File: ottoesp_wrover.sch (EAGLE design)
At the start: 45 parts, among them J1 DC-005, J2 2x3p-2.54, J3 4p-2.54, Q1 S8050, Q2 S8050, Q3 CJ2302, U2 CP2102, U3 CJA1117B-3.3-SOT89, U4 TPD4S012DRYR

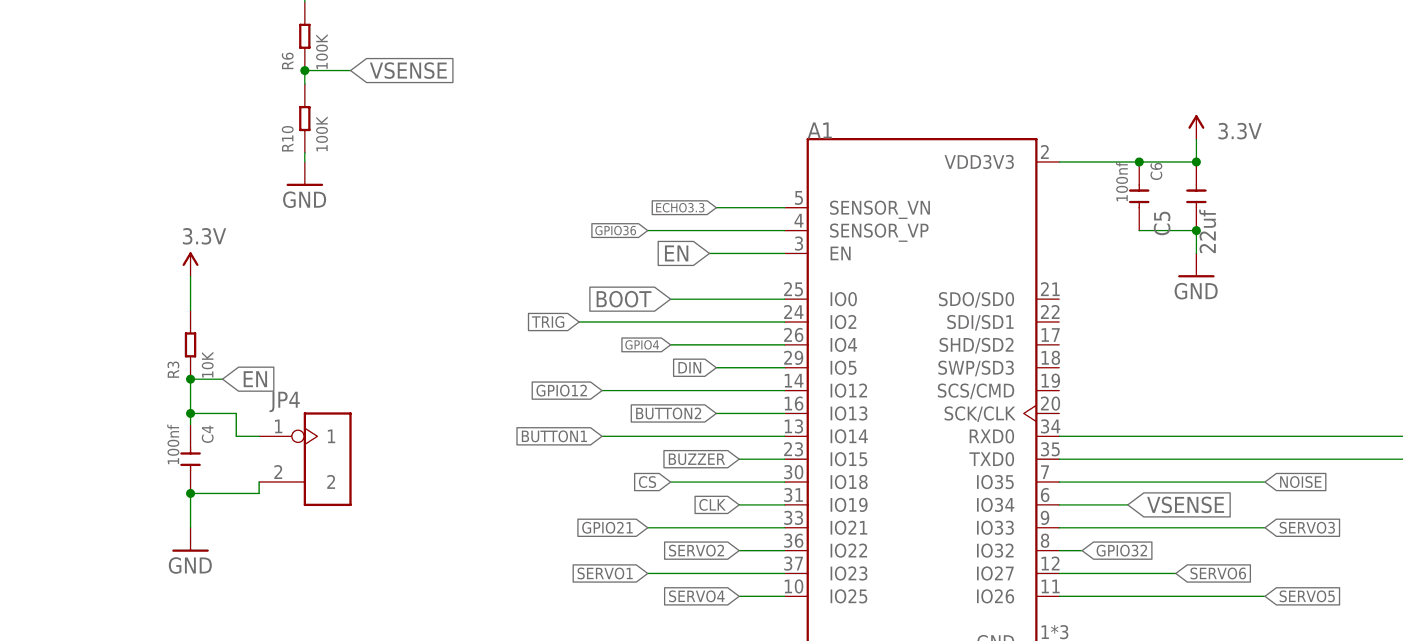
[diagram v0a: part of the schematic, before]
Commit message: Updated cap. These have been produced and seem to work. Still testing
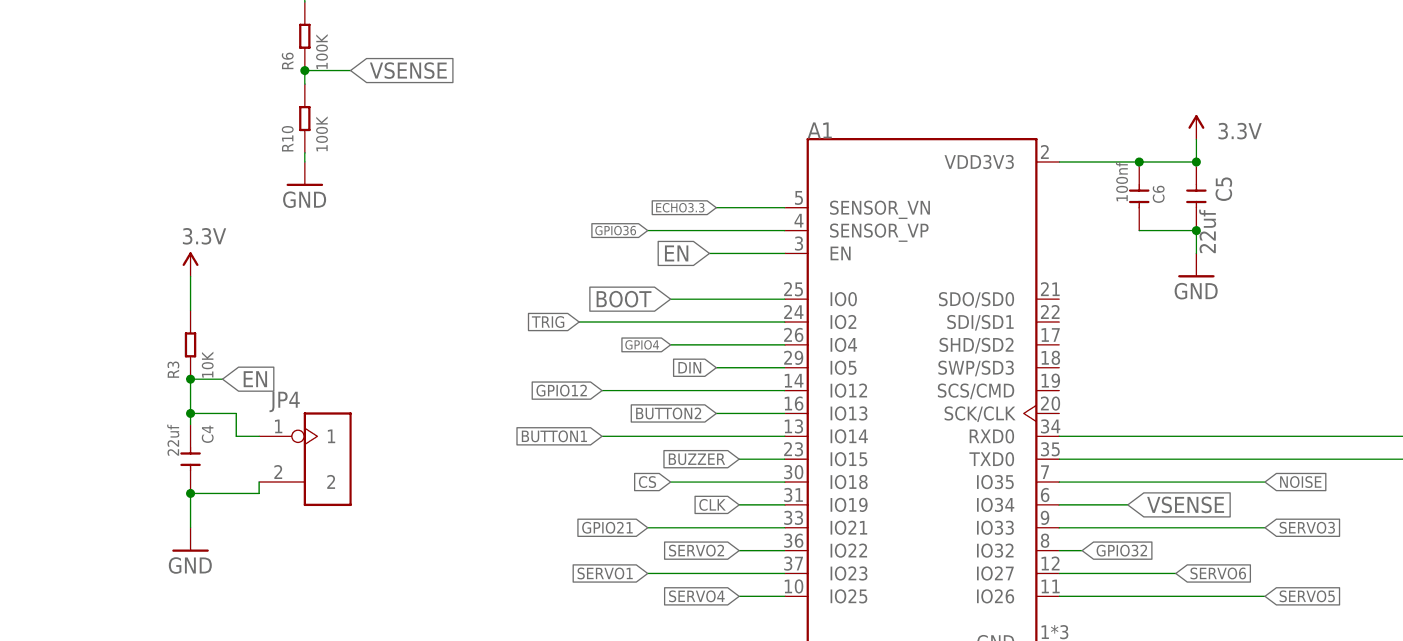
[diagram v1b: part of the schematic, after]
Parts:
- C4: value 100nf -> 22uf
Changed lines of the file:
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@@
 <part name="GND5" library="supply1" deviceset="GND" device=""/>
 <part name="R3" library="OPL_Resistor" library_urn="urn:adsk.eagle:library:8004883" deviceset="SMD-RES-10K-1%-1/8W(0805)" device="" package3d_urn="urn:adsk.eagle:package:8004935/1" value="10K"/>
-<part name="C4" library="OPL_Capacitor" library_urn="urn:adsk.eagle:library:8004261" deviceset="CERAMIC-100NF-50V-10%-X7R(0805)" device="" package3d_urn="urn:adsk.eagle:package:8004286/1" value="100nf"/>
+<part name="C4" library="OPL_Capacitor" library_urn="urn:adsk.eagle:library:8004261" deviceset="CERAMIC-100NF-50V-10%-X7R(0805)" device="" package3d_urn="urn:adsk.eagle:package:8004286/1" value="22uf"/>
 <part name="C5" library="Seeed-Capacitor" deviceset="CERAMIC-22UF-6.3V-20%-X5R(0805)" device="" value="22uf"/>
 <part name="C6" library="OPL_Capacitor" library_urn="urn:adsk.eagle:library:8004261" deviceset="CERAMIC-100NF-50V-10%-X7R(0805)" device="" package3d_urn="urn:adsk.eagle:package:8004286/1" value="100nf"/>
@@
 </instance>
 <instance part="C5" gate="G$1" x="-5.08" y="140.97" smashed="yes" rot="MR270">
-<attribute name="NAME" x="-8.001" y="139.446" size="1.778" layer="95" rot="MR270"/>
+<attribute name="NAME" x="-1.143" y="143.256" size="1.778" layer="95" rot="MR270"/>
 <attribute name="VALUE" x="-2.921" y="139.446" size="1.778" layer="96" rot="MR270"/>
 </instance>
 <instance part="C6" gate="G$1" x="-11.43" y="140.97" smashed="yes" rot="R270">
-<attribute name="NAME" x="-10.16" y="144.78" size="1.27" layer="95" ratio="10" rot="R270"/>
+<attribute name="NAME" x="-9.906" y="142.24" size="1.27" layer="95" ratio="10" rot="R270"/>
 <attribute name="VALUE" x="-13.97" y="144.78" size="1.27" layer="96" ratio="10" rot="R270"/>
 </instance>

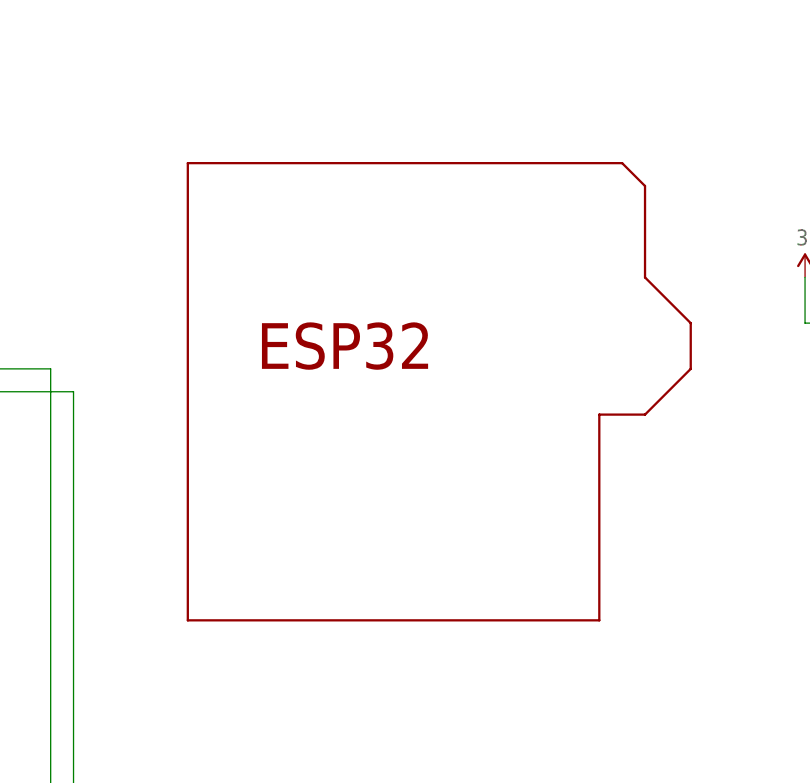
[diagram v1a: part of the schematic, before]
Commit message: Changed to bew PCB with cutout on corner changed cap to 22uf
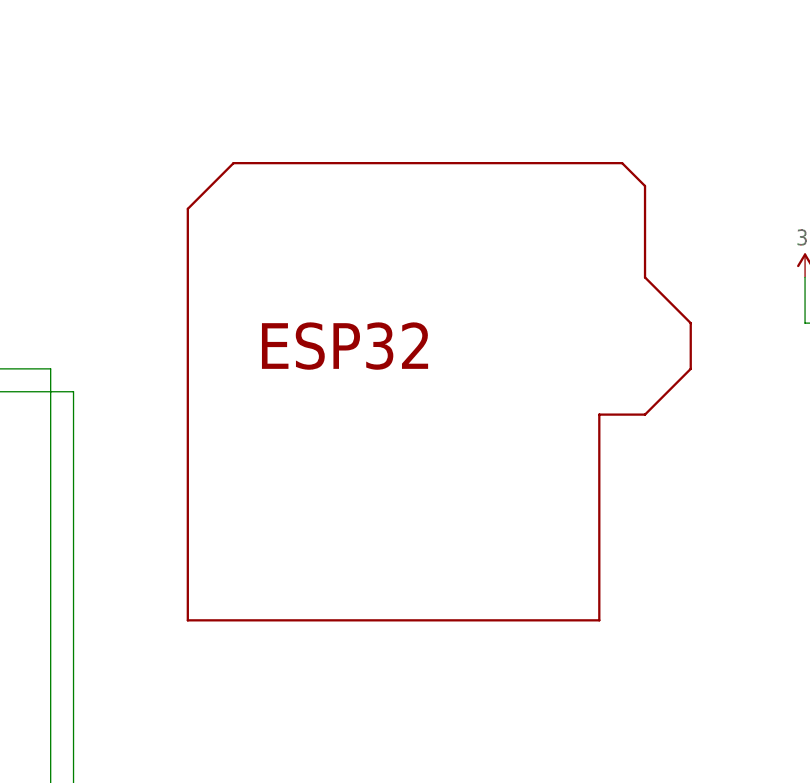
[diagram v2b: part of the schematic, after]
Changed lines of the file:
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@@
 <grid distance="0.1" unitdist="inch" unit="inch" style="lines" multiple="1" display="no" altdistance="0.01" altunitdist="inch" altunit="inch"/>
 <layers>
-<layer number="1" name="Top" color="4" fill="1" visible="no" active="no"/>
-<layer number="2" name="Route2" color="1" fill="3" visible="no" active="no"/>
-<layer number="3" name="Route3" color="4" fill="3" visible="no" active="no"/>
-<layer number="4" name="Route4" color="1" fill="4" visible="no" active="no"/>
-<layer number="5" name="Route5" color="4" fill="4" visible="no" active="no"/>
-<layer number="6" name="Route6" color="1" fill="8" visible="no" active="no"/>
-<layer number="7" name="Route7" color="4" fill="8" visible="no" active="no"/>
-<layer number="8" name="Route8" color="1" fill="2" visible="no" active="no"/>
-<layer number="9" name="Route9" color="4" fill="2" visible="no" active="no"/>
-<layer number="10" name="Route10" color="1" fill="7" visible="no" active="no"/>
-<layer number="11" name="Route11" color="4" fill="7" visible="no" active="no"/>
-<layer number="12" name="Route12" color="1" fill="5" visible="no" active="no"/>
-<layer number="13" name="Route13" color="4" fill="5" visible="no" active="no"/>
-<layer number="14" name="Route14" color="1" fill="6" visible="no" active="no"/>
-<layer number="15" name="Route15" color="4" fill="6" visible="no" active="no"/>
-<layer number="16" name="Bottom" color="1" fill="1" visible="no" active="no"/>
-<layer number="17" name="Pads" color="2" fill="1" visible="no" active="no"/>
-<layer number="18" name="Vias" color="2" fill="1" visible="no" active="no"/>
-<layer number="19" name="Unrouted" color="6" fill="1" visible="no" active="no"/>
-<layer number="20" name="Dimension" color="15" fill="1" visible="no" active="no"/>
-<layer number="21" name="tPlace" color="7" fill="1" visible="no" active="no"/>
-<layer number="22" name="bPlace" color="7" fill="1" visible="no" active="no"/>
-<layer number="23" name="tOrigins" color="15" fill="1" visible="no" active="no"/>
-<layer number="24" name="bOrigins" color="15" fill="1" visible="no" active="no"/>
-<layer number="25" name="tNames" color="7" fill="1" visible="no" active="no"/>
-<layer number="26" name="bNames" color="7" fill="1" visible="no" active="no"/>
-<layer number="27" name="tValues" color="7" fill="1" visible="no" active="no"/>
-<layer number="28" name="bValues" color="7" fill="1" visible="no" active="no"/>
+<layer number="1" name="Top" color="4" fill="1" visible="yes" active="no"/>
+<layer number="2" name="Route2" color="1" fill="3" visible="yes" active="no"/>
+<layer number="3" name="Route3" color="4" fill="3" visible="yes" active="no"/>
+<layer number="4" name="Route4" color="1" fill="4" visible="yes" active="no"/>
+<layer number="5" name="Route5" color="4" fill="4" visible="yes" active="no"/>
+<layer number="6" name="Route6" color="1" fill="8" visible="yes" active="no"/>
+<layer number="7" name="Route7" color="4" fill="8" visible="yes" active="no"/>
+<layer number="8" name="Route8" color="1" fill="2" visible="yes" active="no"/>
+<layer number="9" name="Route9" color="4" fill="2" visible="yes" active="no"/>
+<layer number="10" name="Route10" color="1" fill="7" visible="yes" active="no"/>
+<layer number="11" name="Route11" color="4" fill="7" visible="yes" active="no"/>
+<layer number="12" name="Route12" color="1" fill="5" visible="yes" active="no"/>
+<layer number="13" name="Route13" color="4" fill="5" visible="yes" active="no"/>
+<layer number="14" name="Route14" color="1" fill="6" visible="yes" active="no"/>
+<layer number="15" name="Route15" color="4" fill="6" visible="yes" active="no"/>
+<layer number="16" name="Bottom" color="1" fill="1" visible="yes" active="no"/>
+<layer number="17" name="Pads" color="2" fill="1" visible="yes" active="no"/>
+<layer number="18" name="Vias" color="2" fill="1" visible="yes" active="no"/>
+<layer number="19" name="Unrouted" color="6" fill="1" visible="yes" active="no"/>
+<layer number="20" name="Dimension" color="15" fill="1" visible="yes" active="no"/>
+<layer number="21" name="tPlace" color="7" fill="1" visible="yes" active="no"/>
+<layer number="22" name="bPlace" color="7" fill="1" visible="yes" active="no"/>
+<layer number="23" name="tOrigins" color="15" fill="1" visible="yes" active="no"/>
+<layer number="24" name="bOrigins" color="15" fill="1" visible="yes" active="no"/>
+<layer number="25" name="tNames" color="7" fill="1" visible="yes" active="no"/>
+<layer number="26" name="bNames" color="7" fill="1" visible="yes" active="no"/>
+<layer number="27" name="tValues" color="7" fill="1" visible="yes" active="no"/>
+<layer number="28" name="bValues" color="7" fill="1" visible="yes" active="no"/>
 <layer number="29" name="tStop" color="7" fill="3" visible="no" active="no"/>
 <layer number="30" name="bStop" color="7" fill="6" visible="no" active="no"/>
@@
 <layer number="35" name="tGlue" color="7" fill="4" visible="no" active="no"/>
 <layer number="36" name="bGlue" color="7" fill="5" visible="no" active="no"/>
-<layer number="37" name="tTest" color="7" fill="1" visible="no" active="no"/>
-<layer number="38" name="bTest" color="7" fill="1" visible="no" active="no"/>
+<layer number="37" name="tTest" color="7" fill="1" visible="yes" active="no"/>
+<layer number="38" name="bTest" color="7" fill="1" visible="yes" active="no"/>
 <layer number="39" name="tKeepout" color="4" fill="11" visible="no" active="no"/>
 <layer number="40" name="bKeepout" color="1" fill="11" visible="no" active="no"/>
@@
 <layer number="44" name="Drills" color="7" fill="1" visible="no" active="no"/>
 <layer number="45" name="Holes" color="7" fill="1" visible="no" active="no"/>
-<layer number="46" name="Milling" color="3" fill="1" visible="no" active="no"/>
-<layer number="47" name="Measures" color="7" fill="1" visible="no" active="no"/>
-<layer number="48" name="Document" color="7" fill="1" visible="no" active="no"/>
-<layer number="49" name="Reference" color="7" fill="1" visible="no" active="no"/>
-<layer number="50" name="dxf" color="7" fill="1" visible="no" active="no"/>
-<layer number="51" name="tDocu" color="7" fill="1" visible="no" active="no"/>
-<layer number="52" name="bDocu" color="7" fill="1" visible="no" active="no"/>
-<layer number="53" name="tGND_GNDA" color="7" fill="9" visible="no" active="no"/>
-<layer number="54" name="bGND_GNDA" color="1" fill="9" visible="no" active="no"/>
-<layer number="56" name="wert" color="7" fill="1" visible="no" active="no"/>
-<layer number="57" name="tCAD" color="7" fill="1" visible="no" active="no"/>
-<layer number="59" name="tCarbon" color="7" fill="1" visible="no" active="no"/>
-<layer number="60" name="bCarbon" color="7" fill="1" visible="no" active="no"/>
+<layer number="46" name="Milling" color="3" fill="1" visible="yes" active="no"/>
+<layer number="47" name="Measures" color="7" fill="1" visible="yes" active="no"/>
+<layer number="48" name="Document" color="7" fill="1" visible="yes" active="no"/>
+<layer number="49" name="Reference" color="7" fill="1" visible="yes" active="no"/>
+<layer number="50" name="dxf" color="7" fill="1" visible="yes" active="no"/>
+<layer number="51" name="tDocu" color="7" fill="1" visible="yes" active="no"/>
+<layer number="52" name="bDocu" color="7" fill="1" visible="yes" active="no"/>
+<layer number="53" name="tGND_GNDA" color="7" fill="9" visible="yes" active="no"/>
+<layer number="54" name="bGND_GNDA" color="1" fill="9" visible="yes" active="no"/>
+<layer number="56" name="wert" color="7" fill="1" visible="yes" active="no"/>
+<layer number="57" name="tCAD" color="7" fill="1" visible="yes" active="no"/>
+<layer number="59" name="tCarbon" color="7" fill="1" visible="yes" active="no"/>
+<layer number="60" name="bCarbon" color="7" fill="1" visible="yes" active="no"/>
 <layer number="88" name="SimResults" color="9" fill="1" visible="yes" active="yes"/>
 <layer number="89" name="SimProbes" color="9" fill="1" visible="yes" active="yes"/>
@@
 <part name="P+8" library="supply1" deviceset="V+" device=""/>
 <part name="SUPPLY4" library="SparkFun-Aesthetics" deviceset="3.3V" device=""/>
-<part name="USB1" library="XLibrary" deviceset="ZX62-B-5PA(33)" device="" package3d_urn="urn:adsk.eagle:package:5817502/3" value="ZX62-B-5PA"/>
+<part name="USB1" library="XLibrary" deviceset="ZX62-B-5PA(33)" device="" package3d_urn="urn:adsk.eagle:package:5817502/3" override_package3d_urn="urn:adsk.eagle:package:25338335/2" override_package_urn="urn:adsk.eagle:footprint:25338336/1" value="ZX62-B-5PA"/>
 <part name="GND18" library="supply1" deviceset="GND" device=""/>
 <part name="P+9" library="supply1" deviceset="V+" device=""/>
@@
 <part name="P+1" library="supply1" deviceset="V+" device=""/>
 <part name="P+4" library="supply1" deviceset="V+" device=""/>
-<part name="J1" library="OPL_Connector" library_urn="urn:adsk.eagle:library:8004395" deviceset="CONN-POWER-JACK-2.1MM(DC-005)" device="" package3d_urn="urn:adsk.eagle:package:8004506/1" value="DC-005"/>
+<part name="J1" library="OPL_Connector" library_urn="urn:adsk.eagle:library:8004395" deviceset="CONN-POWER-JACK-2.1MM(DC-005)" device="" package3d_urn="urn:adsk.eagle:package:8004506/1" override_package3d_urn="urn:adsk.eagle:package:25333168/2" override_package_urn="urn:adsk.eagle:footprint:8004472/1" value="DC-005"/>
 <part name="Q3" library="SamacSys_Parts" deviceset="2N7002NXAKR" device="" value="CJ2302"/>
 <part name="P+3" library="supply1" deviceset="V+" device=""/>
@@
 packages will not be understood (or retained) with this version.
 </note>
+<note version="9.4" severity="warning">
+Since Version 9.4, EAGLE supports the overriding of 3D packages
+in schematics and board files. Those overridden 3d packages
+will not be understood (or retained) with this version.
+</note>
 </compatibility>

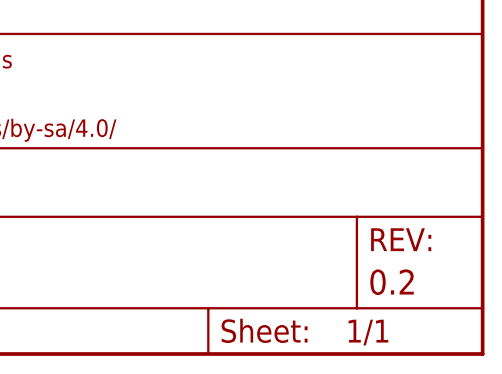
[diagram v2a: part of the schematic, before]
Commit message: Moved the servo pins and some others closer together to allow the use of pin strips.
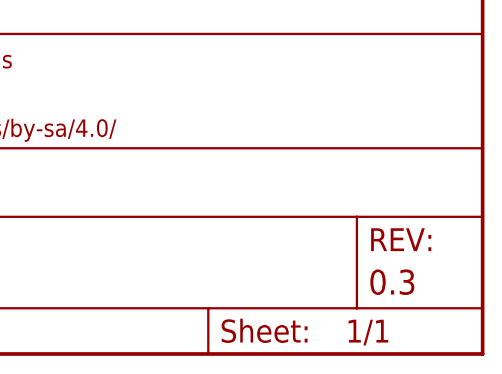
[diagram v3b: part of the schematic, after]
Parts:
- FRAME1: REV 0.2 -> 0.3
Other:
- note added: "12/15/2020"
- note removed: "10/14/2020"

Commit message: Latest board with 3d packages
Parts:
- A1: device ESP32-WROVER-I:ESP32-WROVER-I -> SamacSys_Parts:ESP32-WROVER-I
- C1, C5: device Seeed-Capacitor:CERAMIC-22UF-6.3V-20%-X5R(0805) -> SamacSys_Parts:CERAMIC-22UF-6.3V-20%-X5R(0805)
- C2: device OPL_Capacitor:ALUMINUM-SMD-47UF-25V(D6.3-H5.3MM) -> SamacSys_Parts:ALUMINUM-SMD-47UF-25V(D6.3-H5.3MM)
- C3: device Seeed-Capacitor:CERAMIC-100NF-50V-10%-X7R(0805) -> SamacSys_Parts:CERAMIC-100NF-50V-20%-X5R(0805)
- C4: device OPL_Capacitor:CERAMIC-100NF-50V-10%-X7R(0805) -> SamacSys_Parts:CERAMIC-22UF-6.3V-20%-X5R(0805)
- C6, C9: device OPL_Capacitor:CERAMIC-100NF-50V-10%-X7R(0805) -> SamacSys_Parts:CERAMIC-100NF-50V-20%-X5R(0805)
- C8: device OPL_Capacitor:CERAMIC-4.7UF-25V-10%-X5R(0805) -> SamacSys_Parts:CERAMIC-4.7UF-25V-10%-X5R(0805)
- FRAME1: device SparkFun-Aesthetics:FRAME-LEDGERMISHAFARMS -> SamacSys_Parts:FRAME-LEDGERMISHAFARMS
- J2: device OPL_Connector:DIP-BLACK-MALE-HEADER(2X3P-2.54）-2.54 -> SamacSys_Parts:DIP-BLACK-MALE-HEADER(2X3P-2.54）-2.54
- J3: device OPL_Connector:DIP-BLACK-MALE-HEADER-VERT(4P-2.54) -> SamacSys_Parts:DIP-BLACK-MALE-HEADER-VERT(4P-2.54)
- JP2, JP3, JP4, JP5: device OPL_Connector:DIP-BLACK-MALE-HEADER-VERT(2P-2.54) -> SamacSys_Parts:DIP-BLACK-MALE-HEADER-VERT(2P-2.54)
- JP6: device pinhead:PINHD-1X5 -> SamacSys_Parts:PINHD-1X5
- LA, LF, LL, RF, RL: value Servo -> 3p-2.54; device OPL_Connector:DIP-BLACK-MALE-HEADER-VERT(3P-2.54) -> SamacSys_Parts:DIP-BLACK-MALE-HEADER-VERT(3P-2.54)
- Q1, Q2: value S8050 -> S8050-G; device OPL_Discrete_Semiconductor:SMD-TRANSISTORS-NPN-25V-500MW-S8050(SOT-23) -> SamacSys_Parts:SMD-TRANSISTORS-NPN-25V-500MW-S8050(SOT-23)
- R1, R3, R4, R5: device OPL_Resistor:SMD-RES-10K-1%-1/8W(0805) -> SamacSys_Parts:SMD-RES-10K-1%-1/4W(0805)
- R10, R6: device OPL_Resistor:SMD-RES-100K-1%-1/8W(0805) -> SamacSys_Parts:SMD-RES-100K-.5%-1/10W(0805)
- R2: device OPL_Resistor:SMD-RES-20K-5%-1/8W(0805) -> SamacSys_Parts:SMD-RES-22K-5%-1/4W(0805)
- R7: device OPL_Resistor:SMD-RES-2K-1%-1/8W(0805) -> SamacSys_Parts:SMD-RES-1K-1%-1/8W(0805)
- R8: device OPL_Resistor:SMD-RES-22K-1%-1/8W(0805) -> SamacSys_Parts:SMD-RES-22K-5%-1/4W(0805)
- R9: device OPL_Resistor:SMD-RES-47R-1%-1/8W(0805) -> SamacSys_Parts:SMD-RES-47K-1%-1/4W(0805)
- RA: value Servos -> 3p-2.54; device OPL_Connector:DIP-BLACK-MALE-HEADER-VERT(3P-2.54) -> SamacSys_Parts:DIP-BLACK-MALE-HEADER-VERT(3P-2.54)
- U2: device cp2102:CP2102 -> SamacSys_Parts:CP2102
- USB1: device XLibrary:ZX62-B-5PA(33) -> SamacSys_Parts:ZX62-B-5PA(33)
